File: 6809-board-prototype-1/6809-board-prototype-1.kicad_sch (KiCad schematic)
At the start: 19 parts, among them J1 PWR, U1 MC6809, U2 62256, U3 28C256, U4 16550, U5 74LS04, X1 12MHz, X2 1.8432 MHz

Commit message: actually update the readme
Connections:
- net GND: now also U4.25 (~{ADS}), U4.37 (~{DSR}), U4.38 (~{DCD})
- net at U5.3: now also U4.30 (INTR); no longer U1.3 (~{IRQ})
- net at U5.4: now also U1.3 (~{IRQ}); no longer U4.30 (INTR)
- net at U4.15 (~{BAUDOUT}): now also U4.9 (RCLK)
- no-connect marks 0 -> 7
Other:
- note added: "NOTE: VERIFY NO-CONNECTS, GROUNDED PINS, AND BAUDOUT LOOP WITH DATASHEET"
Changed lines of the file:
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@@
 	)
 	(junction
+		(at 198.12 127)
+		(diameter 0)
+		(color 0 0 0 0)
+	)
+	(junction
 		(at 29.21 71.12)
 		(diameter 0)
@@
 	)
 	(junction
+		(at 270.51 71.12)
+		(diameter 0)
+		(color 0 0 0 0)
+	)
+	(junction
 		(at 29.21 160.02)
 		(diameter 0)
@@
 		(color 0 0 0 0)
 	)
+	(no_connect
+		(at 264.16 88.9)
+	)
+	(no_connect
+		(at 264.16 83.82)
+	)
+	(no_connect
+		(at 264.16 111.76)
+	)
+	(no_connect
+		(at 264.16 66.04)
+	)
+	(no_connect
+		(at 264.16 81.28)
+	)
+	(no_connect
+		(at 264.16 116.84)
+	)
+	(no_connect
+		(at 264.16 114.3)
+	)
 	(bus_entry
 		(at 71.12 87.63)
@@
 	(wire
 		(pts
+			(xy 198.12 127) (xy 198.12 134.62)
+		)
+		(stroke
+			(width 0)
+			(type default)
+		)
+	)
+	(wire
+		(pts
 			(xy 25.4 90.17) (xy 38.1 90.17)
 		)
@@
 	(wire
 		(pts
-			(xy 198.12 124.46) (xy 198.12 125.73)
+			(xy 198.12 124.46) (xy 198.12 127)
 		)
 		(stroke
@@
 	(wire
 		(pts
+			(xy 270.51 72.39) (xy 270.51 71.12)
+		)
+		(stroke
+			(width 0)
+			(type default)
+		)
+	)
+	(wire
+		(pts
 			(xy 50.8 54.61) (xy 50.8 43.18)
 		)
@@
 	(wire
 		(pts
+			(xy 270.51 68.58) (xy 270.51 71.12)
+		)
+		(stroke
+			(width 0)
+			(type default)
+		)
+	)
+	(wire
+		(pts
 			(xy 68.58 85.09) (xy 63.5 85.09)
 		)
@@
 	(wire
 		(pts
+			(xy 270.51 127) (xy 270.51 132.08)
+		)
+		(stroke
+			(width 0)
+			(type default)
+		)
+	)
+	(wire
+		(pts
 			(xy 132.08 59.69) (xy 137.16 59.69)
 		)
@@
 	(wire
 		(pts
+			(xy 198.12 127) (xy 213.36 127)
+		)
+		(stroke
+			(width 0)
+			(type default)
+		)
+	)
+	(wire
+		(pts
 			(xy 116.84 77.47) (xy 111.76 77.47)
 		)
@@
 		)
 	)
+	(wire
+		(pts
+			(xy 264.16 132.08) (xy 270.51 132.08)
+		)
+		(stroke
+			(width 0)
+			(type default)
+		)
+	)
 	(bus
 		(pts
@@
 		)
 	)
+	(wire
+		(pts
+			(xy 264.16 68.58) (xy 270.51 68.58)
+		)
+		(stroke
+			(width 0)
+			(type default)
+		)
+	)
 	(bus
 		(pts
@@
 	(wire
 		(pts
+			(xy 264.16 127) (xy 270.51 127)
+		)
+		(stroke
+			(width 0)
+			(type default)
+		)
+	)
+	(wire
+		(pts
+			(xy 264.16 71.12) (xy 270.51 71.12)
+		)
+		(stroke
+			(width 0)
+			(type default)
+		)
+	)
+	(wire
+		(pts
 			(xy 68.58 64.77) (xy 63.5 64.77)
 		)
@@
 		)
 	)
+	(text "NOTE: VERIFY NO-CONNECTS, \nGROUNDED PINS, AND \nBAUDOUT LOOP WITH DATASHEET"
+		(exclude_from_sim no)
+		(at 265.43 50.8 0)
+		(effects
+			(font
+				(size 1.27 1.27)
+			)
+		)
+	)
 	(text "ROM\n"
 		(exclude_from_sim no)
@@
 		(lib_id "74xx:74LS04")
 		(at 185.42 50.8 90)
-		(mirror x)
 		(unit 2)
 		(exclude_from_sim no)
@@
 		(dnp no)
 		(property "Reference" "U5"
-			(at 180.34 49.5299 90)
+			(at 180.34 52.0701 90)
 			(effects
 				(font
@@
 		)
 		(property "Value" "74LS04"
-			(at 180.34 52.0699 90)
+			(at 180.34 49.5301 90)
 			(effects
 				(font
@@
 	)
 	(symbol
+		(lib_id "power:GNDREF")
+		(at 270.51 72.39 0)
+		(unit 1)
+		(exclude_from_sim no)
+		(in_bom yes)
+		(on_board yes)
+		(dnp no)
+		(fields_autoplaced yes)
+		(property "Reference" "#PWR024"
+			(at 270.51 78.74 0)
+			(effects
+				(font
+					(size 1.27 1.27)
+				)
+				(hide yes)
+			)
+		)
+		(property "Value" "GND"
+			(at 270.51 77.47 0)
+			(effects
+				(font
+					(size 1.27 1.27)
+				)
+				(hide yes)
+			)
+		)
+		(property "Footprint" ""
+			(at 270.51 72.39 0)
+			(effects
+				(font
+					(size 1.27 1.27)
+				)
+				(hide yes)
+			)
+		)
+		(property "Datasheet" ""
+			(at 270.51 72.39 0)
+			(effects
+				(font
+					(size 1.27 1.27)
+				)
+				(hide yes)
+			)
+		)
+		(property "Description" "Power symbol creates a global label with name \"GNDREF\" , reference supply ground"
+			(at 270.51 72.39 0)
+			(effects
+				(font
+					(size 1.27 1.27)
+				)
+				(hide yes)
+			)
+		)
+		(pin "1"
+		)
+		(instances
+			(project "6809-board-prototype-1"
+				(path "/73f02399-4449-4d3e-bf52-6d1b4c7a62b4"
+					(reference "#PWR024")
+					(unit 1)
+				)
+			)
+		)
+	)
+	(symbol
 		(lib_id "Connector:Conn_01x02_Pin")
 		(at 16.51 146.05 0)
@@
 	(symbol
 		(lib_id "power:GNDREF")
-		(at 198.12 125.73 0)
+		(at 198.12 134.62 0)
 		(unit 1)
 		(exclude_from_sim no)
@@
 		(fields_autoplaced yes)
 		(property "Reference" "#PWR015"
-			(at 198.12 132.08 0)
+			(at 198.12 140.97 0)
 			(effects
 				(font
@@
 		)
 		(property "Value" "GND"
-			(at 198.12 130.81 0)
+			(at 198.12 139.7 0)
 			(effects
 				(font
@@
 		)
 		(property "Footprint" ""
-			(at 198.12 125.73 0)
+			(at 198.12 134.62 0)
 			(effects
 				(font
@@
 		)
 		(property "Datasheet" ""
-			(at 198.12 125.73 0)
+			(at 198.12 134.62 0)
 			(effects
 				(font
@@
 		)
 		(property "Description" "Power symbol creates a global label with name \"GNDREF\" , reference supply ground"
-			(at 198.12 125.73 0)
+			(at 198.12 134.62 0)
 			(effects
 				(font

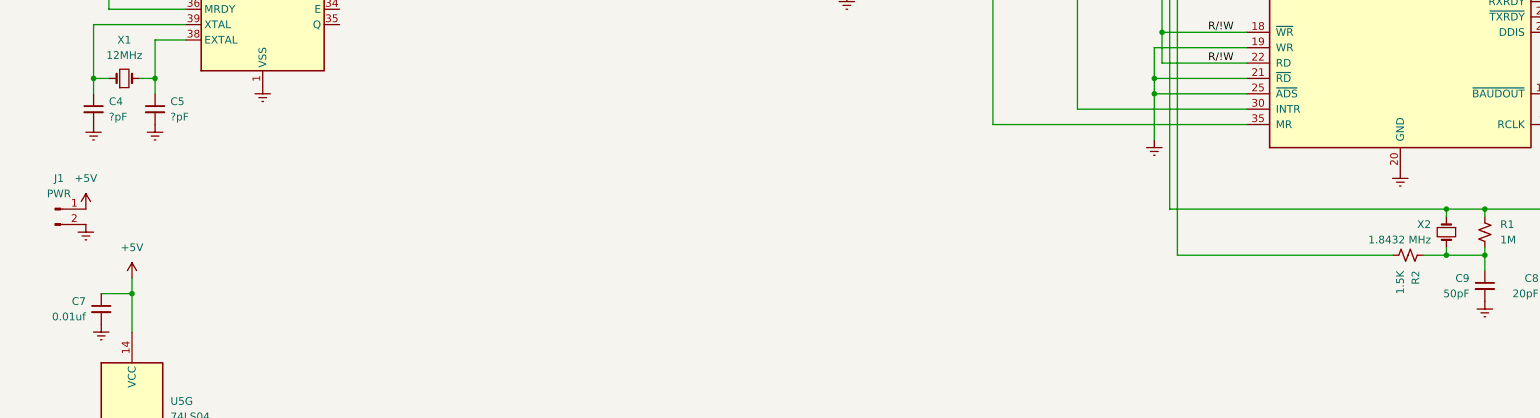
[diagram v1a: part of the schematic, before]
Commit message: VT82C42 info, schematic work. considering moving to cans
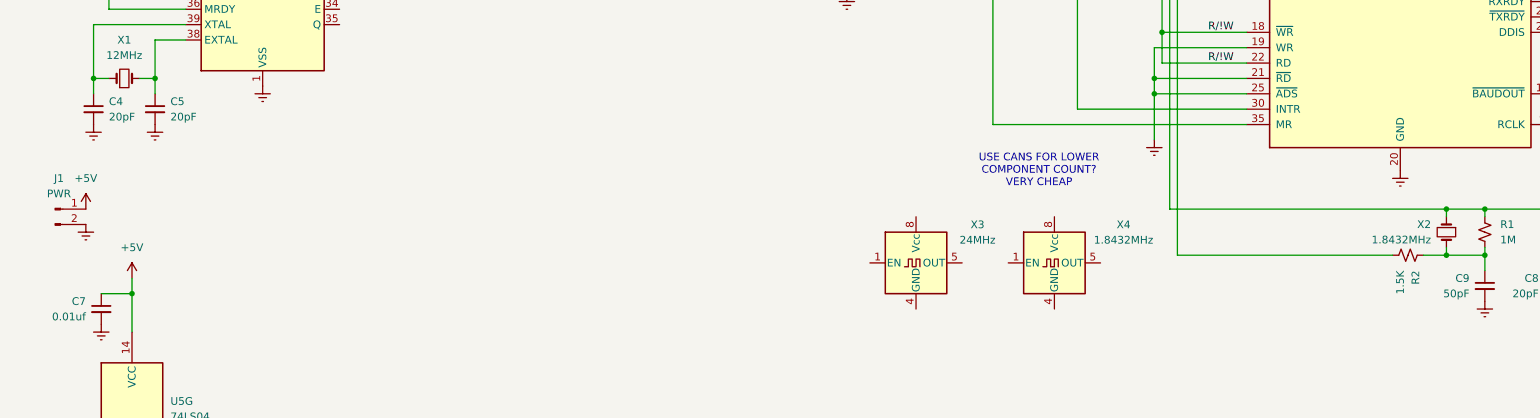
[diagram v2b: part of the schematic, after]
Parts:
- added X3: 24MHz, Oscillator:Oscillator_DIP-8, symbol Oscillator:CXO_DIP8
- added X4: 1.8432MHz, Oscillator:Oscillator_DIP-8, symbol Oscillator:CXO_DIP8
- C4, C5: value ?pF -> 20pF
- X2: value 1.8432 MHz -> 1.8432MHz
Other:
- note added: "USE CANS FOR LOWER COMPONENT COUNT? VERY CHEAP"
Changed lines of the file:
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@@
 		)
 	)
+	(text "USE CANS FOR LOWER\nCOMPONENT COUNT? \nVERY CHEAP"
+		(exclude_from_sim no)
+		(at 179.07 139.7 0)
+		(effects
+			(font
+				(size 1.27 1.27)
+			)
+		)
+	)
 	(text "UART"
 		(exclude_from_sim no)
@@
 	)
 	(symbol
+		(lib_id "Oscillator:CXO_DIP8")
+		(at 158.75 154.94 0)
+		(unit 1)
+		(exclude_from_sim no)
+		(in_bom yes)
+		(on_board yes)
+		(dnp no)
+		(fields_autoplaced yes)
+		(property "Reference" "X3"
+			(at 168.91 148.6214 0)
+			(effects
+				(font
+					(size 1.27 1.27)
+				)
+			)
+		)
+		(property "Value" "24MHz"
+			(at 168.91 151.1614 0)
+			(effects
+				(font
+					(size 1.27 1.27)
+				)
+			)
+		)
+		(property "Footprint" "Oscillator:Oscillator_DIP-8"
+			(at 170.18 163.83 0)
+			(effects
+				(font
+					(size 1.27 1.27)
+				)
+				(hide yes)
+			)
+		)
+		(property "Datasheet" "http://cdn-reichelt.de/documents/datenblatt/B400/OSZI.pdf"
+			(at 156.21 154.94 0)
+			(effects
+				(font
+					(size 1.27 1.27)
+				)
+				(hide yes)
+			)
+		)
+		(property "Description" "Crystal Clock Oscillator, DIP8-style metal package"
+			(at 158.75 154.94 0)
+			(effects
+				(font
+					(size 1.27 1.27)
+				)
+				(hide yes)
+			)
+		)
+		(pin "5"
+		)
+		(pin "4"
+		)
+		(pin "8"
+		)
+		(pin "1"
+		)
+		(instances
+			(project ""
+				(path "/73f02399-4449-4d3e-bf52-6d1b4c7a62b4"
+					(reference "X3")
+					(unit 1)
+				)
+			)
+		)
+	)
+	(symbol
 		(lib_id "power:GNDREF")
 		(at 233.68 48.26 0)
@@
 			)
 		)
-		(property "Value" "?pF"
+		(property "Value" "20pF"
 			(at 25.4 130.8162 0)
 			(effects
@@
 			)
 		)
-		(property "Value" "?pF"
+		(property "Value" "20pF"
 			(at 35.56 130.8162 0)
 			(effects
@@
 	)
 	(symbol
+		(lib_id "Oscillator:CXO_DIP8")
+		(at 181.61 154.94 0)
+		(unit 1)
+		(exclude_from_sim no)
+		(in_bom yes)
+		(on_board yes)
+		(dnp no)
+		(fields_autoplaced yes)
+		(property "Reference" "X4"
+			(at 193.04 148.6214 0)
+			(effects
+				(font
+					(size 1.27 1.27)
+				)
+			)
+		)
+		(property "Value" "1.8432MHz"
+			(at 193.04 151.1614 0)
+			(effects
+				(font
+					(size 1.27 1.27)
+				)
+			)
+		)
+		(property "Footprint" "Oscillator:Oscillator_DIP-8"
+			(at 193.04 163.83 0)
+			(effects
+				(font
+					(size 1.27 1.27)
+				)
+				(hide yes)
+			)
+		)
+		(property "Datasheet" "http://cdn-reichelt.de/documents/datenblatt/B400/OSZI.pdf"
+			(at 179.07 154.94 0)
+			(effects
+				(font
+					(size 1.27 1.27)
+				)
+				(hide yes)
+			)
+		)
+		(property "Description" "Crystal Clock Oscillator, DIP8-style metal package"
+			(at 181.61 154.94 0)
+			(effects
+				(font
+					(size 1.27 1.27)
+				)
+				(hide yes)
+			)
+		)
+		(pin "5"
+		)
+		(pin "4"
+		)
+		(pin "8"
+		)
+		(pin "1"
+		)
+		(instances
+			(project "6809-board-prototype-1"
+				(path "/73f02399-4449-4d3e-bf52-6d1b4c7a62b4"
+					(reference "X4")
+					(unit 1)
+				)
+			)
+		)
+	)
+	(symbol
 		(lib_id "power:+5V")
 		(at 238.76 40.64 0)
@@
 			)
 		)
-		(property "Value" "1.8432 MHz"
+		(property "Value" "1.8432MHz"
 			(at 243.84 151.1299 90)
 			(effects

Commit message: reset switch
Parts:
- added SW1: Reset, symbol Switch:SW_Push_SPDT
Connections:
- net +5V: now also SW1.1 (A)
- net GND: now also SW1.3 (C)
- net /RESET renamed !RESET
- net !RESET: now also SW1.2 (B)
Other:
- note added: "MANUAL RESET SWITCH"

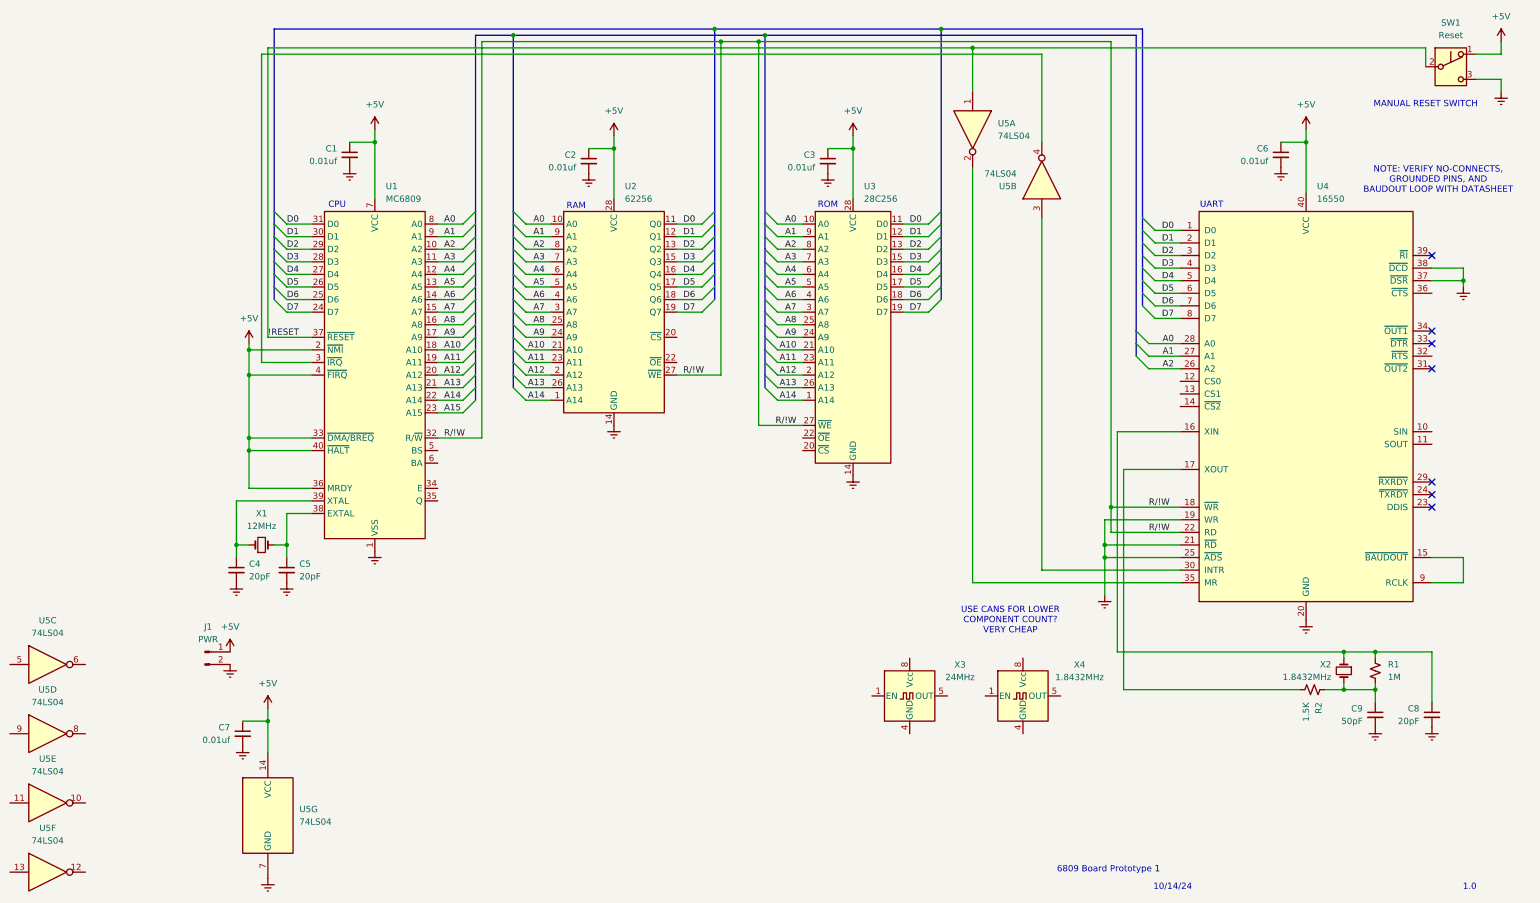
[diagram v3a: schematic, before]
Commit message: set up serial port, new link
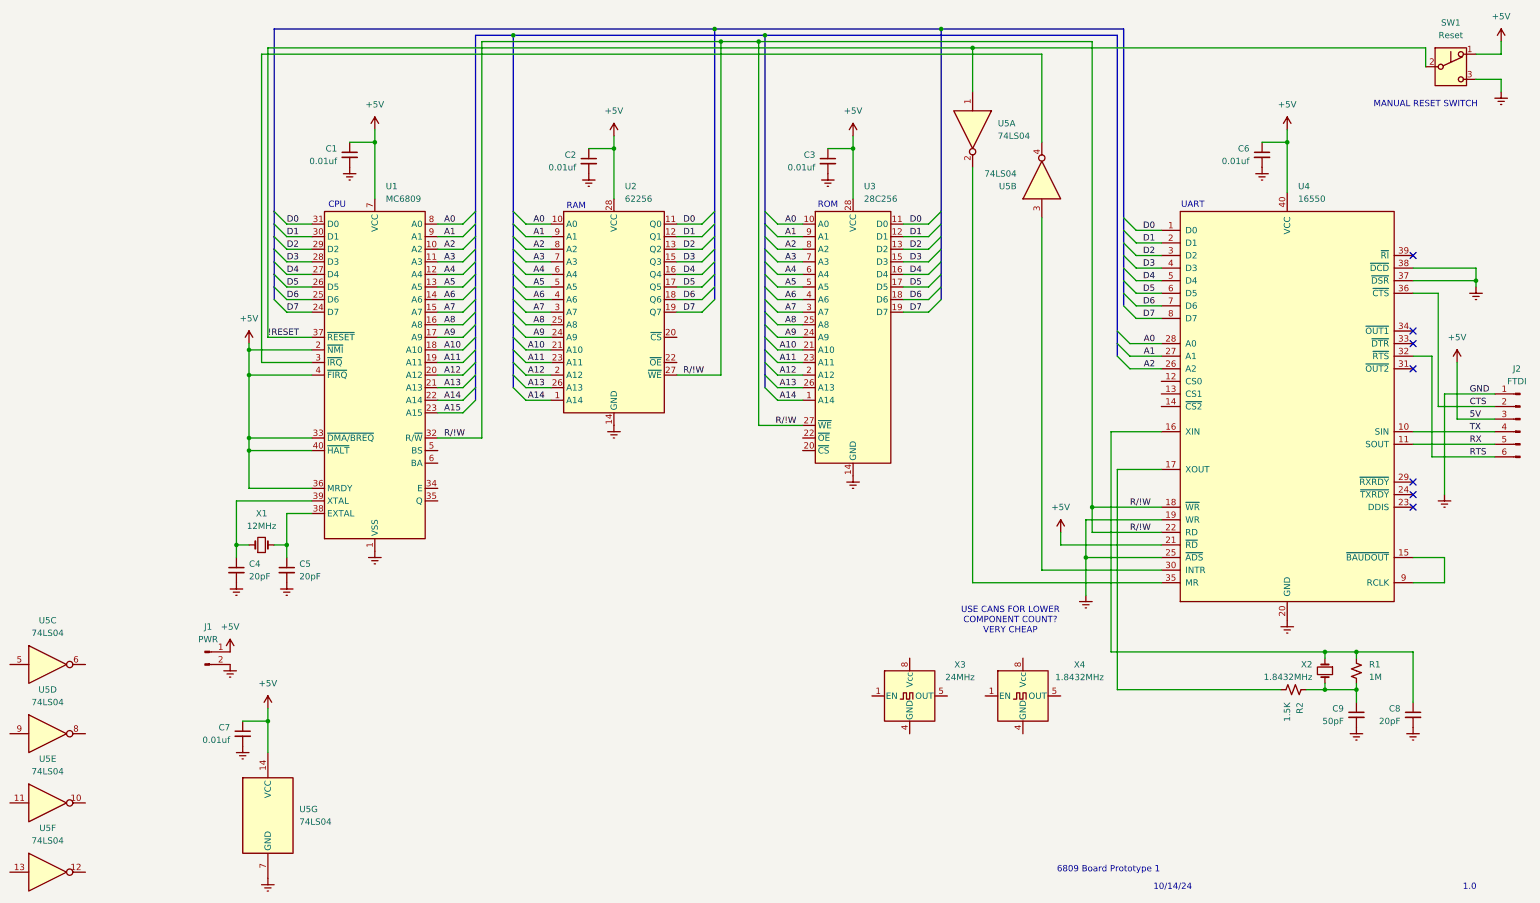
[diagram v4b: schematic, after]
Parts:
- added J2: FTDI, symbol Connector:Conn_01x06_Pin
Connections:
- net +5V: now also U4.21 (~{RD}), J2.3 (Pin_3)
- net GND: now also J2.1 (Pin_1); no longer U4.21 (~{RD})
- net TX: now reaches U4.10 (SIN)
- net TX: now also J2.4 (Pin_4)
- net RX: now reaches U4.11 (SOUT)
- net RX: now also J2.5 (Pin_5)
- net RTS: now reaches U4.32 (~{RTS})
- net RTS: now also J2.6 (Pin_6)
- net CTS: now reaches U4.36 (~{CTS})
- net CTS: now also J2.2 (Pin_2)
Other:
- note removed: "NOTE: VERIFY NO-CONNECTS, GROUNDED PINS, AND BAUDOUT LOOP WITH DATASHEET"
- moved on the sheet: C6, C8, C9, R1, R2, U4, X2
